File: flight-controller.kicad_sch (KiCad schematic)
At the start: 2 parts, among them J1 XT60PW-M

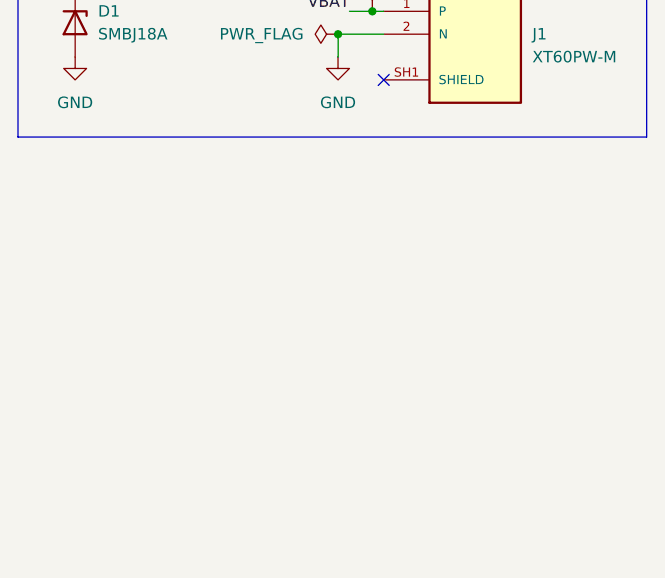
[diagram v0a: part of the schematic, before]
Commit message: feat: Added ACS773
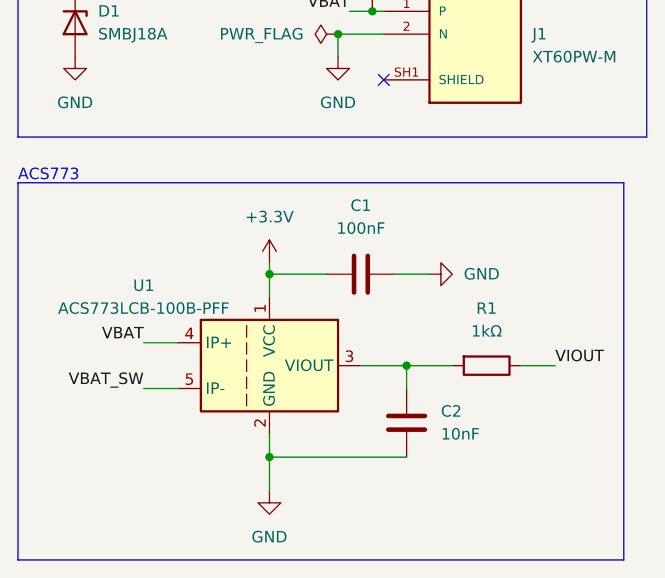
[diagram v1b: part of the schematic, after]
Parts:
- added C1: 100nF, symbol Device:C
- added C2: 10nF, symbol Device:C
- added R1: 1kΩ, symbol Device:R
- added U1: ACS773LCB-100B-PFF, Sensor_Current:Allegro_CB_PFF, symbol Sensor_Current:ACS770xCB-100B-PFF
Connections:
- net GND: now also C1.2, C2.2, U1.2 (GND)
- net VBAT: now also U1.4 (IP+)
- new net: C2.1, R1.2, U1.3 (VIOUT)
- new net +3.3V: C1.1, U1.1 (VCC)
- new net VBAT_SW: U1.5 (IP-)
- new net VIOUT: R1.1
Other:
- note added: "ACS773"
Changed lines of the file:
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@@
   (junction (at 57.15 33.02) (diameter 0) (color 0 0 0 0)
   )
+  (junction (at 64.77 69.85) (diameter 0) (color 0 0 0 0)
+  )
+  (junction (at 49.53 59.69) (diameter 0) (color 0 0 0 0)
+  )
+  (junction (at 49.53 80.01) (diameter 0) (color 0 0 0 0)
+  )
   (junction (at 60.96 30.48) (diameter 0) (color 0 0 0 0)
   )
   (no_connect (at 62.23 38.1))
+  (wire (pts (xy 49.53 77.47) (xy 49.53 80.01))
+    (stroke (width 0) (type default))
+  )
+  (wire (pts (xy 49.53 80.01) (xy 49.53 83.82))
+    (stroke (width 0) (type default))
+  )
   (wire (pts (xy 27.94 26.67) (xy 27.94 27.94))
     (stroke (width 0) (type default))
   )
+  (wire (pts (xy 49.53 58.42) (xy 49.53 59.69))
+    (stroke (width 0) (type default))
+  )
+  (wire (pts (xy 35.56 67.31) (xy 39.37 67.31))
+    (stroke (width 0) (type default))
+  )
+  (wire (pts (xy 35.56 72.39) (xy 39.37 72.39))
+    (stroke (width 0) (type default))
+  )
   (wire (pts (xy 62.23 33.02) (xy 57.15 33.02))
     (stroke (width 0) (type default))
   )
+  (wire (pts (xy 64.77 69.85) (xy 69.85 69.85))
+    (stroke (width 0) (type default))
+  )
+  (wire (pts (xy 49.53 59.69) (xy 49.53 62.23))
+    (stroke (width 0) (type default))
+  )
+  (wire (pts (xy 49.53 59.69) (xy 55.88 59.69))
+    (stroke (width 0) (type default))
+  )
   (wire (pts (xy 60.96 30.48) (xy 62.23 30.48))
     (stroke (width 0) (type default))
@@
     (stroke (width 0) (type default))
   )
+  (wire (pts (xy 59.69 69.85) (xy 64.77 69.85))
+    (stroke (width 0) (type default))
+  )
+  (wire (pts (xy 49.53 80.01) (xy 64.77 80.01))
+    (stroke (width 0) (type default))
+  )
+  (wire (pts (xy 64.77 69.85) (xy 64.77 72.39))
+    (stroke (width 0) (type default))
+  )
+  (wire (pts (xy 63.5 59.69) (xy 67.31 59.69))
+    (stroke (width 0) (type default))
+  )
+  (wire (pts (xy 77.47 69.85) (xy 81.28 69.85))
+    (stroke (width 0) (type default))
+  )
   (wire (pts (xy 57.15 33.02) (xy 57.15 35.56))
     (stroke (width 0) (type default))
@@
     (stroke (width 0) (type default))
     (fill (type none))
+  )
+  (rectangle (start 21.59 49.53) (end 88.9 91.44)
+    (stroke (width 0) (type default))
+    (fill (type none))
+  )
+  (text "ACS773" (at 21.59 49.53 0)
+    (effects (font (size 1.27 1.27)) (justify left bottom))
   )
   (text "BATTERY_CONNECTOR" (at 21.59 21.59 0)
     (effects (font (size 1.27 1.27)) (justify left bottom))
   )
+  (label "VBAT" (at 35.56 67.31 180) (fields_autoplaced)
+    (effects (font (size 1.27 1.27)) (justify right bottom))
+  )
   (label "VBAT" (at 58.42 30.48 180) (fields_autoplaced)
     (effects (font (size 1.27 1.27)) (justify right bottom))
   )
+  (label "VIOUT" (at 81.28 69.85 0) (fields_autoplaced)
+    (effects (font (size 1.27 1.27)) (justify left bottom))
+  )
+  (label "VBAT_SW" (at 35.56 72.39 180) (fields_autoplaced)
+    (effects (font (size 1.27 1.27)) (justify right bottom))
+  )
   (label "VBAT" (at 27.94 26.67 0) (fields_autoplaced)
     (effects (font (size 1.27 1.27)) (justify left bottom))
   )
+  (symbol (lib_id "power:GND") (at 49.53 83.82 0) (unit 1)
+    (in_bom yes) (on_board yes) (dnp no) (fields_autoplaced)
+    (property "Reference" "#PWR03" (at 49.53 90.17 0)
+      (effects (font (size 1.27 1.27)) hide)
+    )
+    (property "Value" "GND" (at 49.53 88.9 0)
+      (effects (font (size 1.27 1.27)))
+    )
+    (property "Footprint" "" (at 49.53 83.82 0)
+      (effects (font (size 1.27 1.27)) hide)
+    )
+    (property "Datasheet" "" (at 49.53 83.82 0)
+      (effects (font (size 1.27 1.27)) hide)
+    )
+    (pin "1")
+    (instances
+      (project "flight-controller"
+        (path "/cfde3d0f-a989-480c-bca2-a8bde2d458df"
+          (reference "#PWR03") (unit 1)
+        )
+      )
+    )
+  )
+  (symbol (lib_id "Device:R") (at 73.66 69.85 270) (unit 1)
+    (in_bom yes) (on_board yes) (dnp no) (fields_autoplaced)
+    (property "Reference" "R1" (at 73.66 63.5 90)
+      (effects (font (size 1.27 1.27)))
+    )
+    (property "Value" "1kΩ" (at 73.66 66.04 90)
+      (effects (font (size 1.27 1.27)))
+    )
+    (property "Footprint" "" (at 73.66 68.072 90)
+      (effects (font (size 1.27 1.27)) hide)
+    )
+    (property "Datasheet" "~" (at 73.66 69.85 0)
+      (effects (font (size 1.27 1.27)) hide)
+    )
+    (pin "2")
+    (pin "1")
+    (instances
+      (project "flight-controller"
+        (path "/cfde3d0f-a989-480c-bca2-a8bde2d458df"
+          (reference "R1") (unit 1)
+        )
+      )
+    )
+  )
   (symbol (lib_id "Device:D_Zener") (at 27.94 31.75 270) (unit 1)
     (in_bom yes) (on_board yes) (dnp no) (fields_autoplaced)
@@
     )
   )
+  (symbol (lib_id "Device:C") (at 59.69 59.69 90) (unit 1)
+    (in_bom yes) (on_board yes) (dnp no) (fields_autoplaced)
+    (property "Reference" "C1" (at 59.69 52.07 90)
+      (effects (font (size 1.27 1.27)))
+    )
+    (property "Value" "100nF" (at 59.69 54.61 90)
+      (effects (font (size 1.27 1.27)))
+    )
+    (property "Footprint" "" (at 63.5 58.7248 0)
+      (effects (font (size 1.27 1.27)) hide)
+    )
+    (property "Datasheet" "~" (at 59.69 59.69 0)
+      (effects (font (size 1.27 1.27)) hide)
+    )
+    (pin "1")
+    (pin "2")
+    (instances
+      (project "flight-controller"
+        (path "/cfde3d0f-a989-480c-bca2-a8bde2d458df"
+          (reference "C1") (unit 1)
+        )
+      )
+    )
+  )
   (symbol (lib_id "Custom_BEC_PS:XT60PW-M") (at 72.39 33.02 0) (unit 1)
     (in_bom yes) (on_board yes) (dnp no) (fields_autoplaced)
@@
     )
   )
+  (symbol (lib_id "power:+3.3V") (at 49.53 58.42 0) (unit 1)
+    (in_bom yes) (on_board yes) (dnp no) (fields_autoplaced)
+    (property "Reference" "#PWR04" (at 49.53 62.23 0)
+      (effects (font (size 1.27 1.27)) hide)
+    )
+    (property "Value" "+3.3V" (at 49.53 53.34 0)
+      (effects (font (size 1.27 1.27)))
+    )
+    (property "Footprint" "" (at 49.53 58.42 0)
+      (effects (font (size 1.27 1.27)) hide)
+    )
+    (property "Datasheet" "" (at 49.53 58.42 0)
+      (effects (font (size 1.27 1.27)) hide)
+    )
+    (pin "1")
+    (instances
+      (project "flight-controller"
+        (path "/cfde3d0f-a989-480c-bca2-a8bde2d458df"
+          (reference "#PWR04") (unit 1)
+        )
+      )
+    )
+  )
   (symbol (lib_id "power:PWR_FLAG") (at 57.15 33.02 90) (unit 1)
     (in_bom yes) (on_board yes) (dnp no) (fields_autoplaced)
@@
         )
       )
+    )
+  )
+  (symbol (lib_id "Device:C") (at 64.77 76.2 0) (unit 1)
+    (in_bom yes) (on_board yes) (dnp no) (fields_autoplaced)
+    (property "Reference" "C2" (at 68.58 74.93 0)
+      (effects (font (size 1.27 1.27)) (justify left))
+    )
+    (property "Value" "10nF" (at 68.58 77.47 0)
+      (effects (font (size 1.27 1.27)) (justify left))
+    )
+    (property "Footprint" "" (at 65.7352 80.01 0)
+      (effects (font (size 1.27 1.27)) hide)
+    )
+    (property "Datasheet" "~" (at 64.77 76.2 0)
+      (effects (font (size 1.27 1.27)) hide)
+    )
+    (pin "1")
+    (pin "2")
+    (instances
+      (project "flight-controller"
+        (path "/cfde3d0f-a989-480c-bca2-a8bde2d458df"
+          (reference "C2") (unit 1)
+        )
+      )
+    )
+  )
+  (symbol (lib_id "Sensor_Current:ACS770xCB-100B-PFF") (at 49.53 69.85 0) (unit 1)
+    (in_bom yes) (on_board yes) (dnp no)
+    (property "Reference" "U1" (at 35.56 60.96 0)
+      (effects (font (size 1.27 1.27)))
+    )
+    (property "Value" "ACS773LCB-100B-PFF" (at 35.56 63.5 0)
+      (effects (font (size 1.27 1.27)))
+    )
+    (property "Footprint" "Sensor_Current:Allegro_CB_PFF" (at 49.53 69.85 0)
+      (effects (font (size 1.27 1.27)) hide)
+    )
+    (property "Datasheet" "http://www.allegromicro.com/~/media/Files/Datasheets/ACS758-Datasheet.ashx?la=en" (at 49.53 69.85 0)
+      (effects (font (size 1.27 1.27)) hide)
+    )
+    (pin "4")
+    (pin "3")
+    (pin "2")
+    (pin "5")
+    (pin "1")
+    (instances
+      (project "flight-controller"
+        (path "/cfde3d0f-a989-480c-bca2-a8bde2d458df"
+          (reference "U1") (unit 1)
+        )
+      )
+    )
+  )
+  (symbol (lib_id "power:GND") (at 67.31 59.69 90) (unit 1)
+    (in_bom yes) (on_board yes) (dnp no) (fields_autoplaced)
+    (property "Reference" "#PWR05" (at 73.66 59.69 0)
+      (effects (font (size 1.27 1.27)) hide)
+    )
+    (property "Value" "GND" (at 71.12 59.69 90)
+      (effects (font (size 1.27 1.27)) (justify right))
+    )
+    (property "Footprint" "" (at 67.31 59.69 0)
+      (effects (font (size 1.27 1.27)) hide)
+    )
+    (property "Datasheet" "" (at 67.31 59.69 0)
+      (effects (font (size 1.27 1.27)) hide)
+    )
+    (pin "1")
+    (instances
+      (project "flight-controller"
+        (path "/cfde3d0f-a989-480c-bca2-a8bde2d458df"
+          (reference "#PWR05") (unit 1)
+        )
+      )

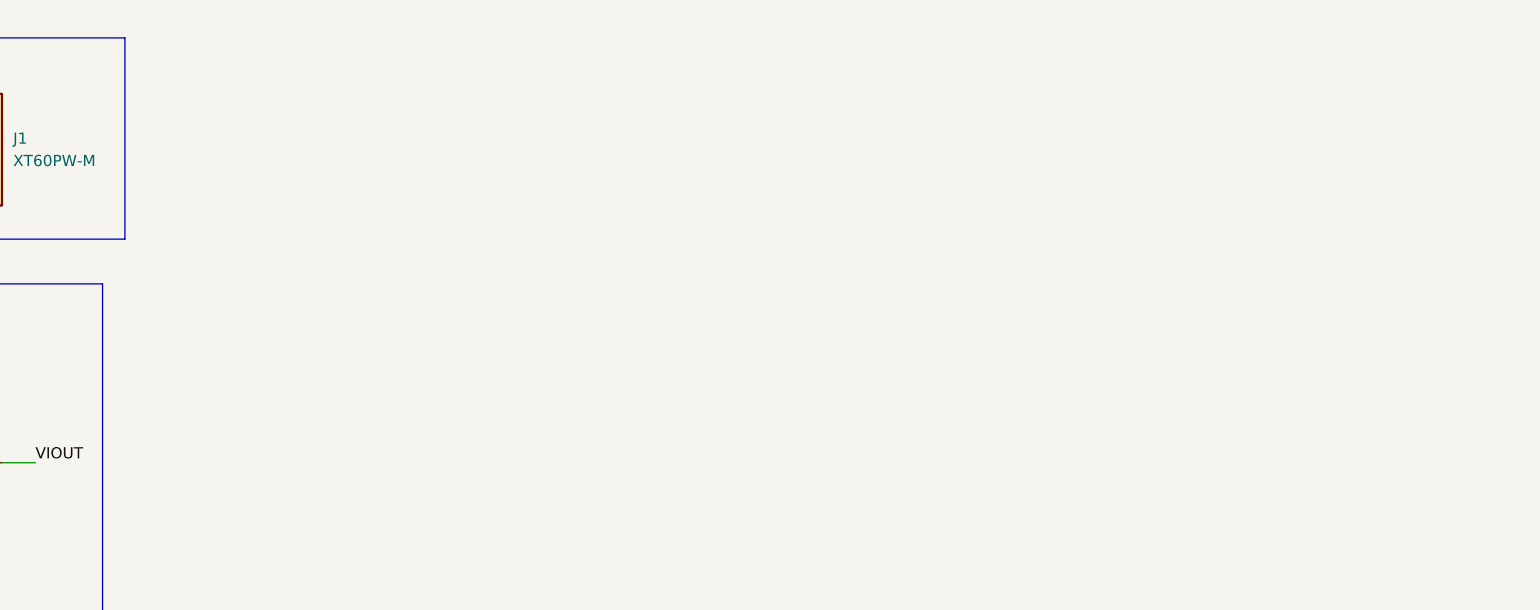
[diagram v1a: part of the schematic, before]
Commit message: feat: Added buck converter
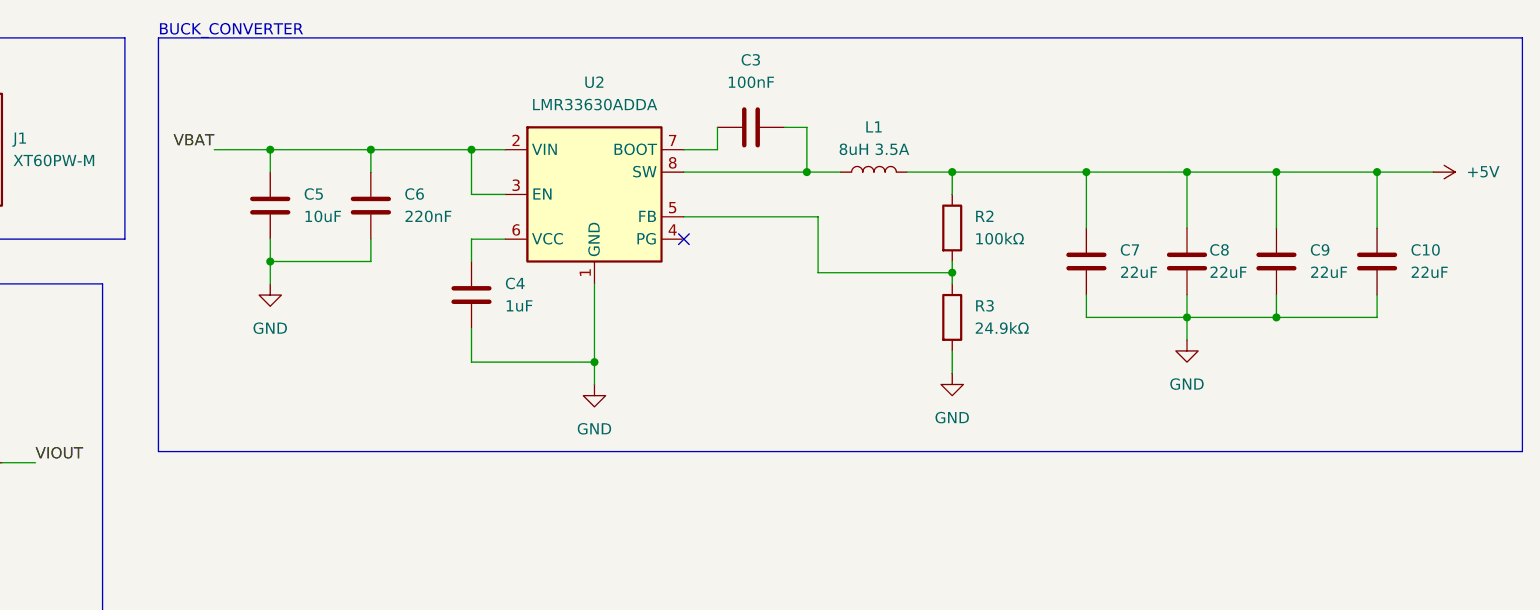
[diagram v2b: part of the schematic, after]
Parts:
- added C10, C7, C8, C9: 22uF, symbol Device:C
- added C3: 100nF, symbol Device:C
- added C4: 1uF, symbol Device:C
- added C5: 10uF, symbol Device:C
- added C6: 220nF, symbol Device:C
- added L1: 8uH 3.5A, symbol Device:L
- added R2: 100kΩ, symbol Device:R
- added R3: 24.9kΩ, symbol Device:R
- added U2: LMR33630ADDA, Package_SO:Texas_HSOP-8-1EP_3.9x4.9mm_P1.27mm_ThermalVias, symbol Regulator_Switching:LMR33630ADDA
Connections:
- net GND: now also C10.2, C4.2, C5.2, C6.2, C7.2, C8.2, C9.2, R3.2, U2.1 (GND), U2.9 (GND)
- net VBAT: now also C5.1, C6.1, U2.2 (VIN), U2.3 (EN)
- new net: C3.1, U2.7 (BOOT)
- new net: C3.2, L1.1, U2.8 (SW)
- new net: C4.1, U2.6 (VCC)
- new net: R2.2, R3.1, U2.5 (FB)
- new net +5V: C10.1, C7.1, C8.1, C9.1, L1.2, R2.1
- no-connect marks 1 -> 2
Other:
- note added: "BUCK_CONVERTER"

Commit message: chore: Assigned footprints to components
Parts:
- C1, C2, C3, C4, C6: footprint (none) -> Capacitor_SMD:C_0805_2012Metric
- C10, C7, C8, C9: footprint (none) -> Capacitor_SMD:C_1210_3225Metric
- C5: footprint (none) -> Capacitor_SMD:C_1206_3216Metric
- L1: footprint (none) -> Inductor_SMD:L_Bourns_SRR1260
- R1, R2, R3: footprint (none) -> Resistor_SMD:R_0805_2012Metric
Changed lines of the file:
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@@
       (effects (font (size 1.27 1.27)) (justify left))
     )
-    (property "Footprint" "" (at 108.9152 44.45 0)
+    (property "Footprint" "Capacitor_SMD:C_1206_3216Metric" (at 108.9152 44.45 0)
       (effects (font (size 1.27 1.27)) hide)
     )
@@
       (effects (font (size 1.27 1.27)))
     )
-    (property "Footprint" "" (at 166.37 30.7848 0)
+    (property "Footprint" "Capacitor_SMD:C_0805_2012Metric" (at 166.37 30.7848 0)
       (effects (font (size 1.27 1.27)) hide)
     )
@@
       (effects (font (size 1.27 1.27)))
     )
-    (property "Footprint" "" (at 176.53 36.83 0)
+    (property "Footprint" "Inductor_SMD:L_Bourns_SRR1260" (at 176.53 36.83 0)
       (effects (font (size 1.27 1.27)) hide)
     )
@@
       (effects (font (size 1.27 1.27)))
     )
-    (property "Footprint" "" (at 73.66 68.072 90)
+    (property "Footprint" "Resistor_SMD:R_0805_2012Metric" (at 73.66 68.072 90)
       (effects (font (size 1.27 1.27)) hide)
     )
@@
       (effects (font (size 1.27 1.27)) (justify left))
     )
-    (property "Footprint" "" (at 213.0552 50.8 0)
+    (property "Footprint" "Capacitor_SMD:C_1210_3225Metric" (at 213.0552 50.8 0)
       (effects (font (size 1.27 1.27)) hide)
     )
@@
       (effects (font (size 1.27 1.27)) (justify left))
     )
-    (property "Footprint" "" (at 201.6252 50.8 0)
+    (property "Footprint" "Capacitor_SMD:C_1210_3225Metric" (at 201.6252 50.8 0)
       (effects (font (size 1.27 1.27)) hide)
     )
@@
       (effects (font (size 1.27 1.27)) (justify left))
     )
-    (property "Footprint" "" (at 131.7752 54.61 0)
+    (property "Footprint" "Capacitor_SMD:C_0805_2012Metric" (at 131.7752 54.61 0)
       (effects (font (size 1.27 1.27)) hide)
     )
@@
       (effects (font (size 1.27 1.27)))
     )
-    (property "Footprint" "" (at 63.5 58.7248 0)
+    (property "Footprint" "Capacitor_SMD:C_0805_2012Metric" (at 63.5 58.7248 0)
       (effects (font (size 1.27 1.27)) hide)
     )
@@
       (effects (font (size 1.27 1.27)) (justify left))
     )
-    (property "Footprint" "" (at 223.2152 50.8 0)
+    (property "Footprint" "Capacitor_SMD:C_1210_3225Metric" (at 223.2152 50.8 0)
       (effects (font (size 1.27 1.27)) hide)
     )
@@
       (effects (font (size 1.27 1.27)) (justify bottom) hide)
     )
-    (property "Datasheet" "" (at 72.39 33.02 0)
+    (property "Datasheet" "~" (at 72.39 33.02 0)
       (effects (font (size 1.27 1.27)) hide)
     )
@@
       (effects (font (size 1.27 1.27)) (justify left))
     )
-    (property "Footprint" "" (at 120.3452 44.45 0)
+    (property "Footprint" "Capacitor_SMD:C_0805_2012Metric" (at 120.3452 44.45 0)
       (effects (font (size 1.27 1.27)) hide)
     )
@@
       (effects (font (size 1.27 1.27)) (justify left))
     )
-    (property "Footprint" "" (at 183.642 53.34 90)
+    (property "Footprint" "Resistor_SMD:R_0805_2012Metric" (at 183.642 53.34 90)
       (effects (font (size 1.27 1.27)) hide)
     )
@@
       (effects (font (size 1.27 1.27)) (justify left))
     )
-    (property "Footprint" "" (at 65.7352 80.01 0)
+    (property "Footprint" "Capacitor_SMD:C_0805_2012Metric" (at 65.7352 80.01 0)
       (effects (font (size 1.27 1.27)) hide)
     )
@@
       (effects (font (size 1.27 1.27)) (justify left))
     )
-    (property "Footprint" "" (at 234.6452 50.8 0)
+    (property "Footprint" "Capacitor_SMD:C_1210_3225Metric" (at 234.6452 50.8 0)
       (effects (font (size 1.27 1.27)) hide)
     )
@@
       (effects (font (size 1.27 1.27)) (justify left))
     )
-    (property "Footprint" "" (at 183.642 43.18 90)
-      (effects (font (size 1.27 1.27)) hide)
-    )
+    (property "Footprint" "Resistor_SMD:R_0805_2012Metric" (at 183.642 43.18 90)
+      (effects (font (size 1.27 1.27)) hide)
+    )
